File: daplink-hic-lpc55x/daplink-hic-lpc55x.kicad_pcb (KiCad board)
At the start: 4 copper layers, 43.2 x 35.6 mm, 41 parts, among them J1 Conn_01x12_Socket, J2 Conn_01x12_Socket, SW2 SW_Push, U1 LPC55x16JEV98E, Y1 ABM8-16.000MHZ-B2-T

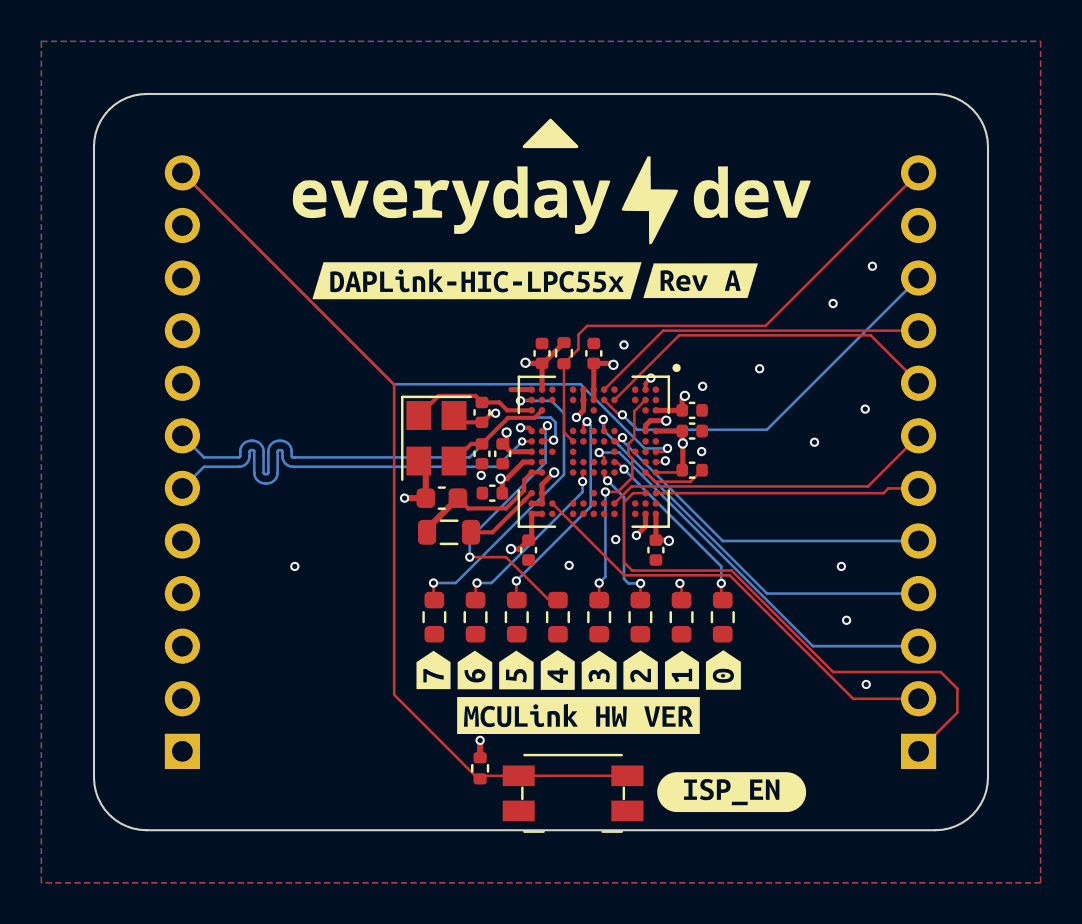
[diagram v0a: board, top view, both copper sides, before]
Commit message: Update LPC package to the 100LQFP
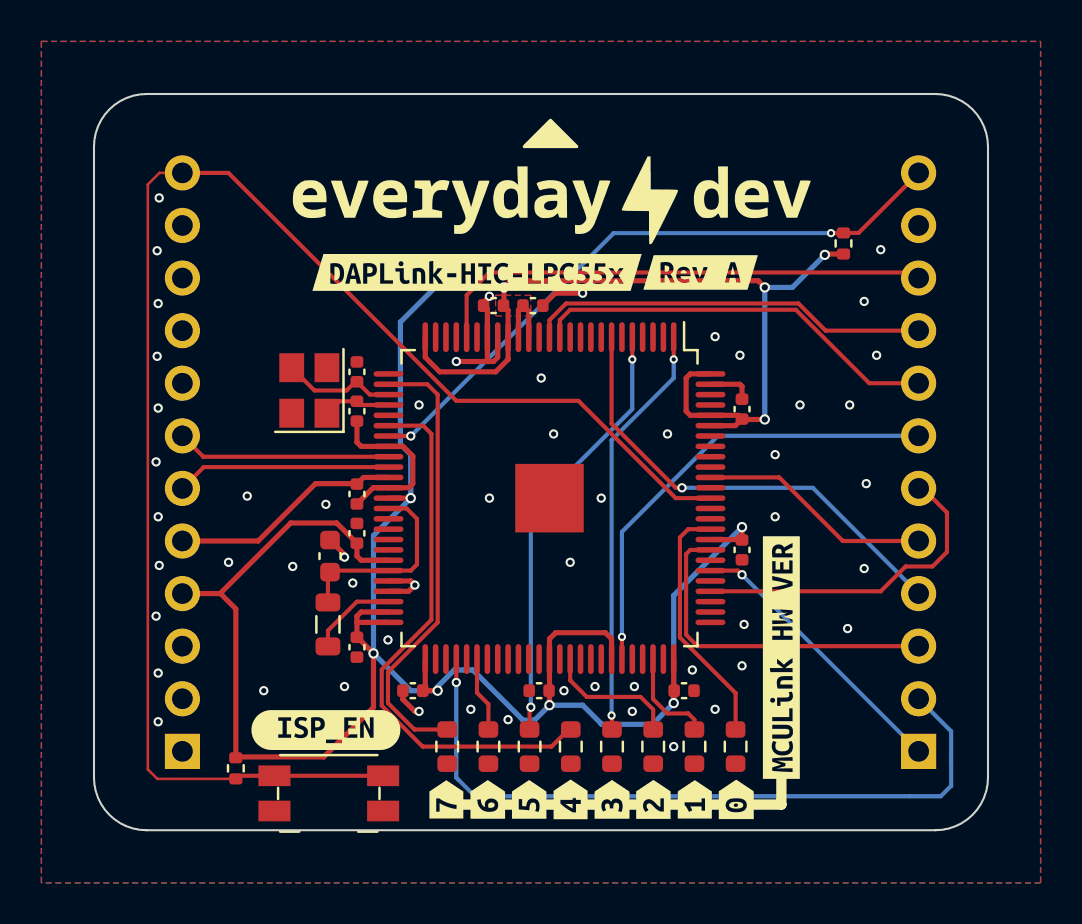
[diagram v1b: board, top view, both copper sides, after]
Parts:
- removed C14: 22u, Capacitor_SMD:C_0603_1608Metric
- removed C16: 0.1u, Capacitor_SMD:C_0402_1005Metric
- removed U1: LPC55x16JEV98E, usb-dev:BGA-98_13x13_7.0x7.0mm
- added C10: 0.1u, Capacitor_SMD:C_0402_1005Metric, F.Cu at (137.9, 78.4)
- added C11: 0.1u, Capacitor_SMD:C_0402_1005Metric, F.Cu at (119.3, 83.1)
- added C9: 22u, Capacitor_SMD:C_0603_1608Metric, F.Cu at (118.0, 78.7)
- added U2: LPC55x16JBD100, daplink-hic-lpc55x:QFP-100_14x14_Pitch0.5mm, F.Cu at (128.6, 75.9)
- moved kibuzzard-6554FF4C 19.8 mm to (117.8, 87.1)
- moved C4 17.2 mm to (119.3, 77.6), turned to -90 degrees
- moved R1 14.5 mm to (142.8, 63.6), turned to 90 degrees
- moved C2 12.2 mm to (122.0, 85.2), turned to 0 degrees
- moved SW2 11.8 mm to (117.9, 90.2)
- moved R2 11.8 mm to (113.5, 89.0)
- moved C5 11.3 mm to (125.9, 66.6), turned to 0 degrees
- moved C1 10.7 mm to (135.1, 85.2)
- moved kibuzzard-656792B8 10.2 mm to (139.8, 83.6), turned to 90 degrees
- moved C6 10.0 mm to (137.9, 71.6)
- moved C3 8.83 mm to (128.1, 85.2), turned to 0 degrees
- moved L1 7.35 mm to (117.9, 82.0), turned to -90 degrees
- moved C15 7.22 mm to (119.3, 69.8), turned to -90 degrees
- moved Y1 6.56 mm to (117.0, 70.7), turned to 90 degrees
- moved C7 6.54 mm to (119.3, 75.7), turned to 90 degrees
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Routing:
- net +3V3: track 74.6 -> 146.3 mm, vias 8 -> 10
- net /HIC_USB_P: track 24.6 -> 10.4 mm, vias 1 -> 0
- net /TGT_TCK_SWCLK: track 21.6 -> 35.1 mm, vias 0 -> 1
- net /HW_VER_4: track 13.4 -> 26.7 mm, vias 2 -> 0
- net /TGT_TMS_SWDIO: track 26.6 -> 13.7 mm, vias 0 -> 1
- net /HIC_USB_N: track 21.6 -> 10.4 mm, vias 1 -> 0
- net /HW_VER_5: track 10.6 -> 21.0 mm
- net /HW_VER_3: track 11.0 -> 20.2 mm
- net VBUS: track 19.2 -> 11.2 mm, vias 1 -> 0
- net GND: track 17.2 -> 24.5 mm, vias 23 -> 55
- net /HW_VER_7: track 15.1 -> 21.9 mm, vias 2 -> 0
- net /TGT_UART_TX: track 16.0 -> 22.4 mm, vias 0 -> 1
- net /HIC_TDO_SWO: track 18.8 -> 24.4 mm, vias 1 -> 0
- net /TGT_nRESET_OUT: track 16.9 -> 11.3 mm, vias 1 -> 0
- net /HIC_nRESET: track 25.3 -> 30.9 mm, vias 0 -> 2
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- added copper zone on F.Cu, net +3V3
- removed copper zone on In1.Cu, net GND
- removed copper zone on In2.Cu, net GND
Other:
- copper layers 4 -> 2
